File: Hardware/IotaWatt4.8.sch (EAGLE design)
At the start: 59 parts, among them J0 2.1MMJACKSMT, J1 STEREO_SMD, J10 STEREO_SMD, J11 STEREO_SMD, J12 STEREO_SMD, J13 STEREO_SMD, J14 STEREO_SMD, J2 STEREO_SMD, J3 STEREO_SMD, J4 STEREO_SMD, J5 STEREO_SMD, J6 STEREO_SMD, J7 STEREO_SMD, J8 STEREO_SMD, J9 STEREO_SMD, Y1 32Khz

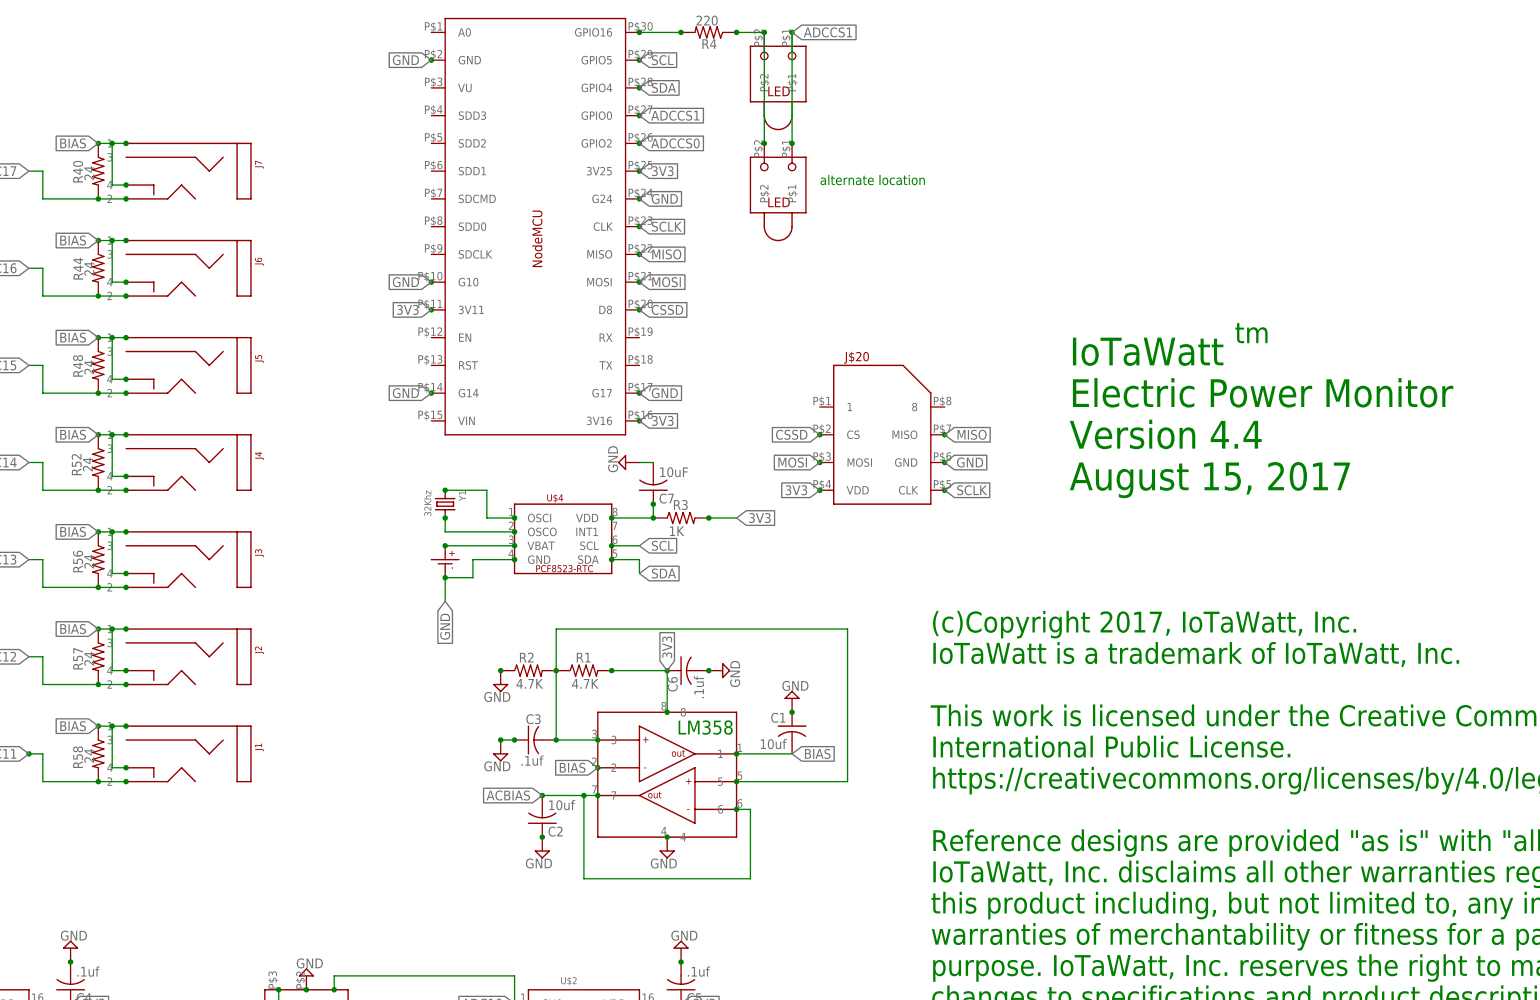
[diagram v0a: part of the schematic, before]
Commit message: Update to latest version 4.8
Remove extra LED mounting position
Reroute traces around SDcard to eliminate mfg problems
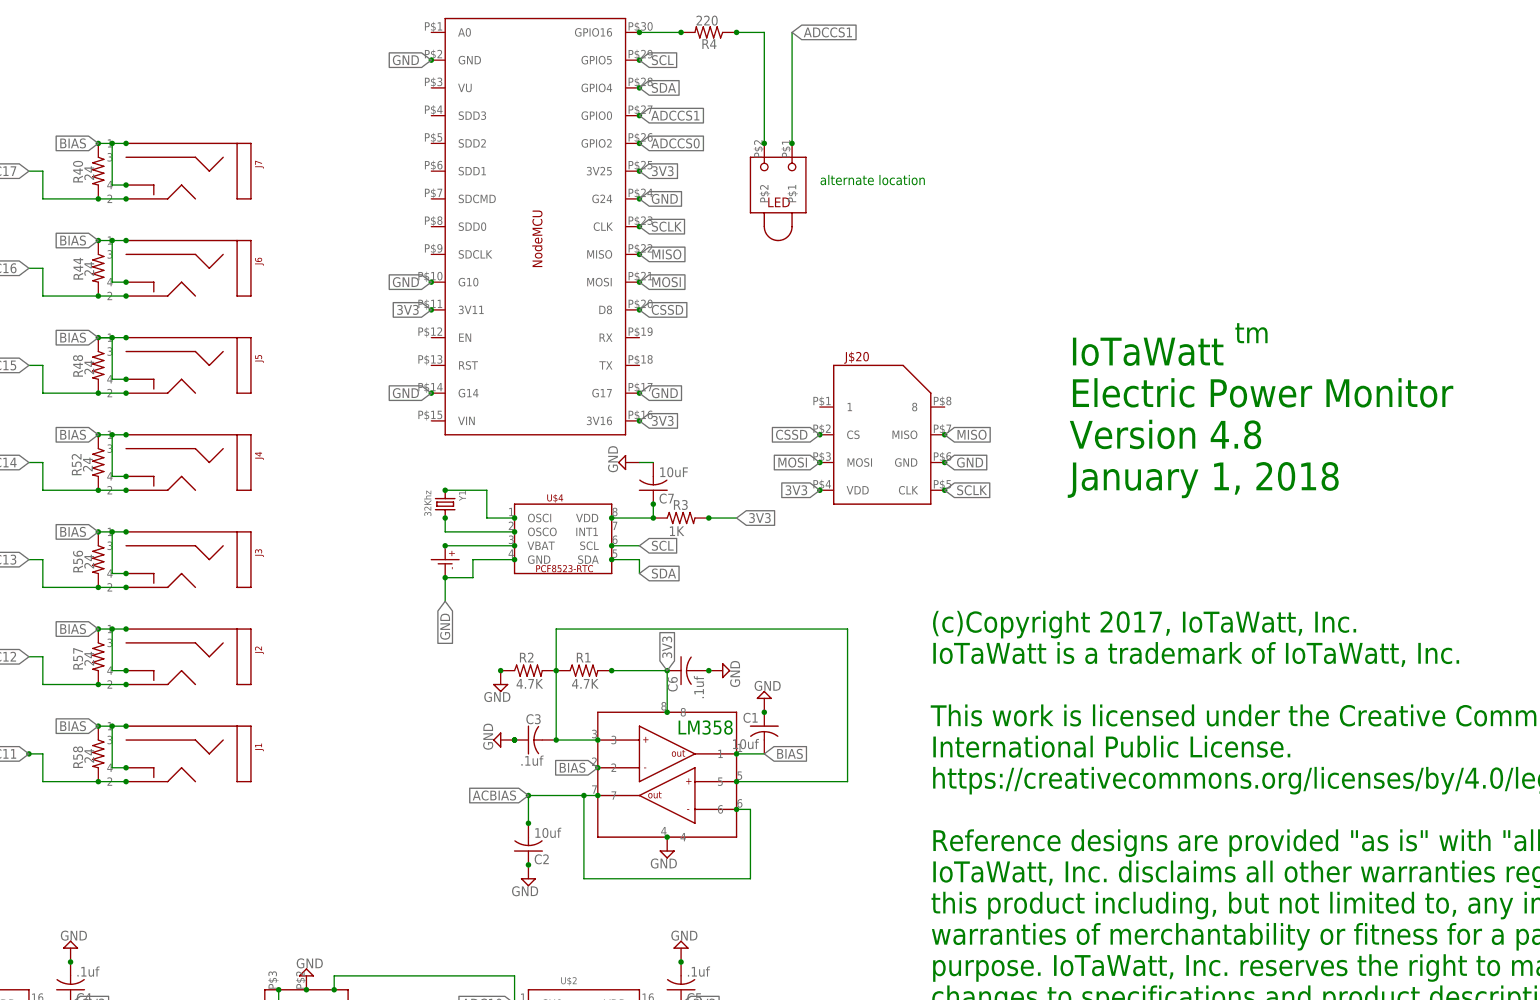
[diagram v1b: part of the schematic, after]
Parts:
- removed U$15: LED_RT_TRH, IotaWatt_parts:LED_RT_TRH
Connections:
- net ADCCS1: no longer U$15.P$1
- net N$8: no longer U$15.P$2
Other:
- note added: "IoTaWatt Electric Power Monitor Version 4.8 January 1, 2018"
- note removed: "IoTaWatt Electric Power Monitor Version 4.4 August 15, 2017"
- moved on the sheet: C1, C2
